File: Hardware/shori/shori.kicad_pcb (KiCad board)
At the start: 4 copper layers, 93 x 39.4 mm, 54 parts, among them J1 Conn_02x03_Top_Bottom, J2 SWD_Header, J3 UART_Header, J5 AudioJack3, U1 STM32F405RGT6, U2 AP2112K-3.3, U3 PCM3060PWR, U4 NE5532, Y1 16MHz

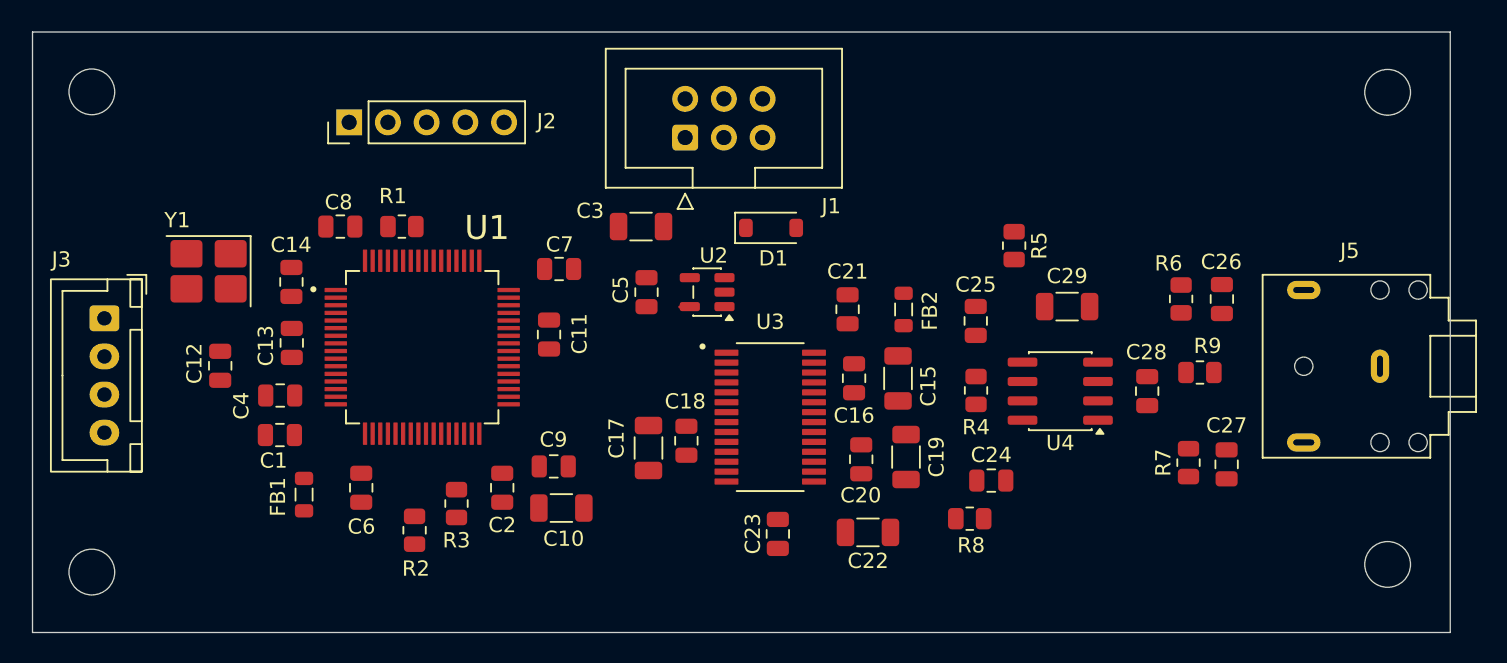
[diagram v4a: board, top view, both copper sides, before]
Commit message: Routes Oscillator, Gamen and Programming header.
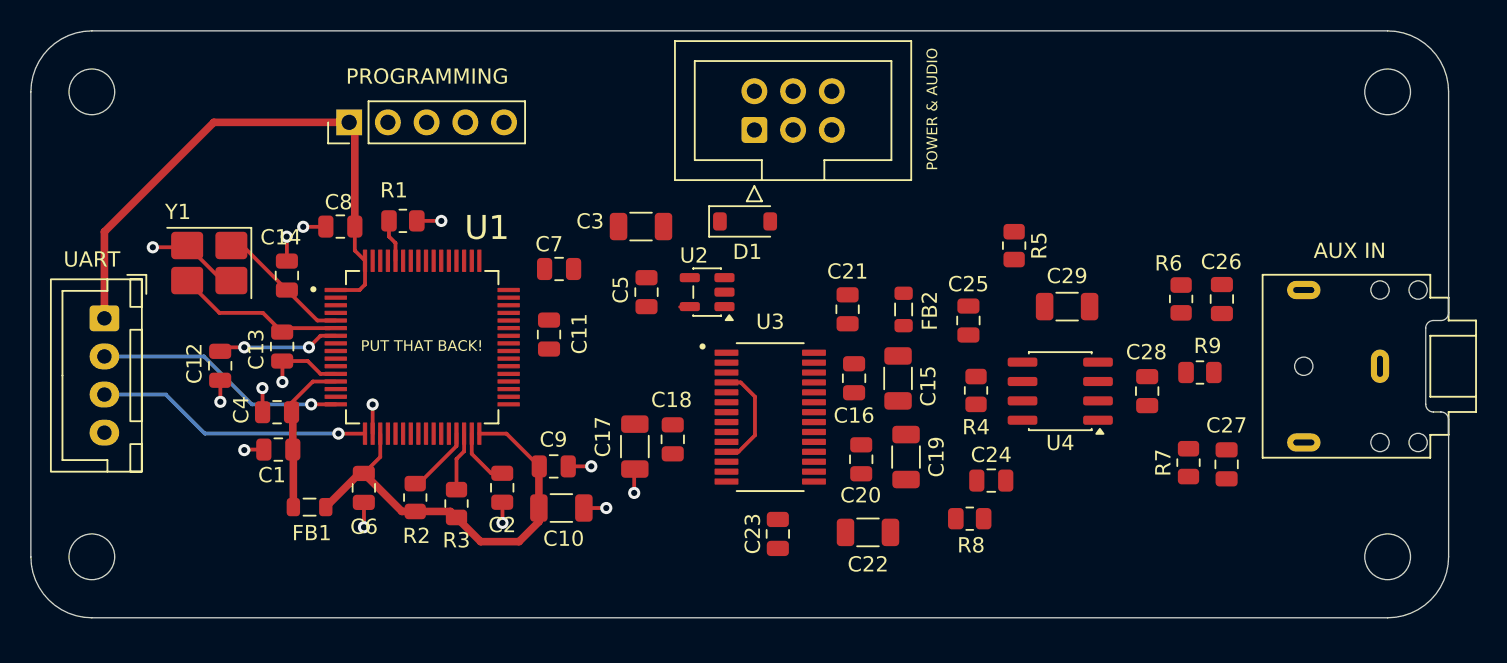
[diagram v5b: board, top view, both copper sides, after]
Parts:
- AUX IN: renamed from J5
- POWER & AUDIO: renamed from J1
- moved POWER & AUDIO 4.57 mm to (153.0, 74.5)
- moved R2 2.15 mm to (130.7, 98.6)
- moved D1 1.76 mm to (152.3, 80.5)
- moved C4 1.11 mm to (121.7, 93.0)
- moved H4 1.00 mm to (109.5, 102.5)
- moved C1 0.96 mm to (121.7, 95.5)
- moved C18 0.90 mm to (147.6, 94.8)
- moved C17 0.90 mm to (145.1, 95.3)
- moved FB1 0.90 mm to (123.8, 99.2), turned to 180 degrees
- moved C13 0.67 mm to (122.0, 88.7)
- moved Y1 0.54 mm to (117.2, 83.2)
- moved C14 0.51 mm to (122.3, 84.0)
- moved H2 0.50 mm to (194.5, 102.5)
- moved C25 0.48 mm to (167.0, 87.0)
- moved R1 0.38 mm to (129.9, 80.5)
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- renumbered J2 to PROGRAMMING, J3 to UART
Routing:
- net +3.3V: track 0.71 -> 67.4 mm
- net GND: track 0.00 -> 29.9 mm, vias 0 -> 14
- net /UART_RX: track 0.00 -> 18.2 mm, vias 0 -> 1
- net /UART_TX: track 0.00 -> 16.5 mm, vias 0 -> 1
- net /LOAD_CAP13: track 0.00 -> 10.9 mm
- net +3.3VA: track 0.00 -> 10.2 mm
- net /LOAD_CAP14: track 0.00 -> 8.89 mm
- net /NRST: track 0.00 -> 8.00 mm, vias 0 -> 2
- net /I2S_LRCLK: track 0.00 -> 7.11 mm
- net /I2C_SCL: track 0.00 -> 4.54 mm
- net /I2C_SDA: track 0.00 -> 3.88 mm
- net /VCAP_1: track 0.00 -> 3.85 mm
- net /BOOT0_R: track 0.00 -> 2.79 mm
- added copper zone on In1.Cu, net GND
- added copper zone on In2.Cu, net GND
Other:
- board size 93 x 39.4 mm -> 93 x 38.5 mm
- board text added: "PUT THAT BACK!"

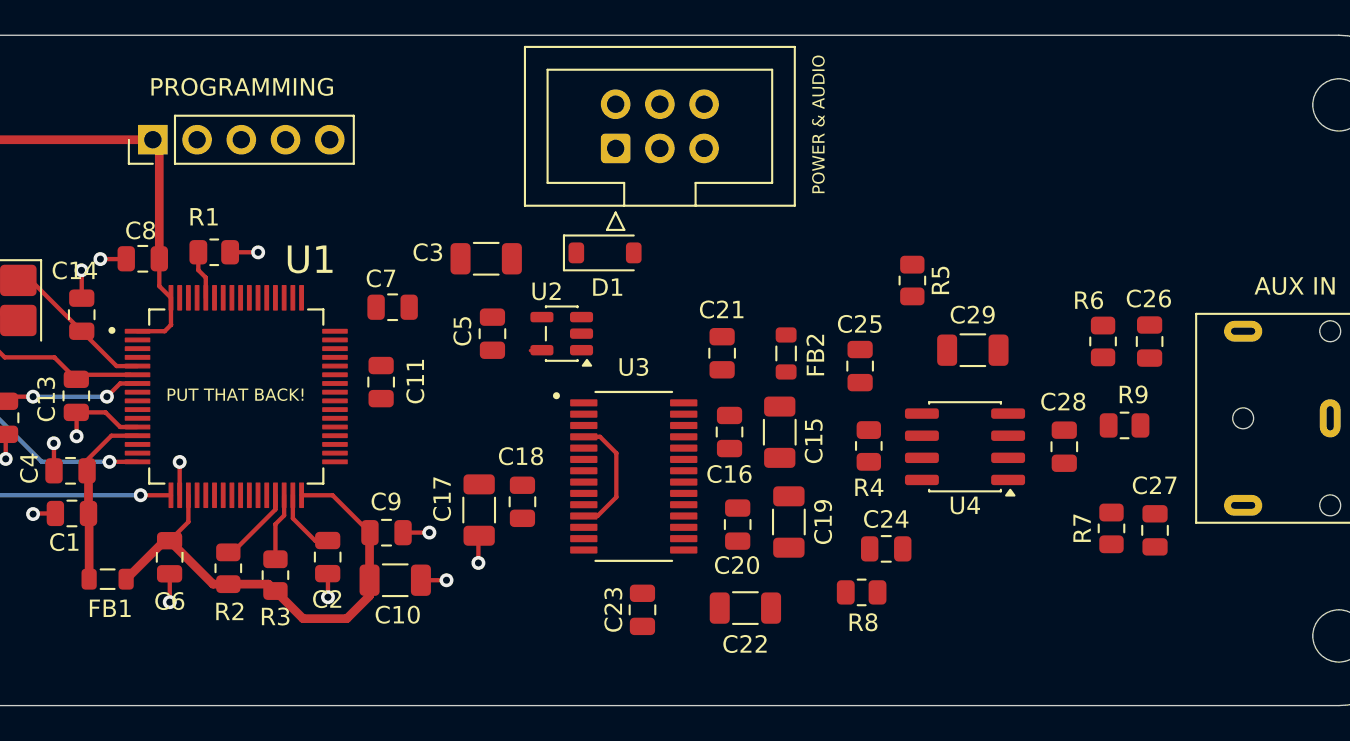
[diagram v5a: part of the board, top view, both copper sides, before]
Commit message: Rough Analog Routing complete for shori
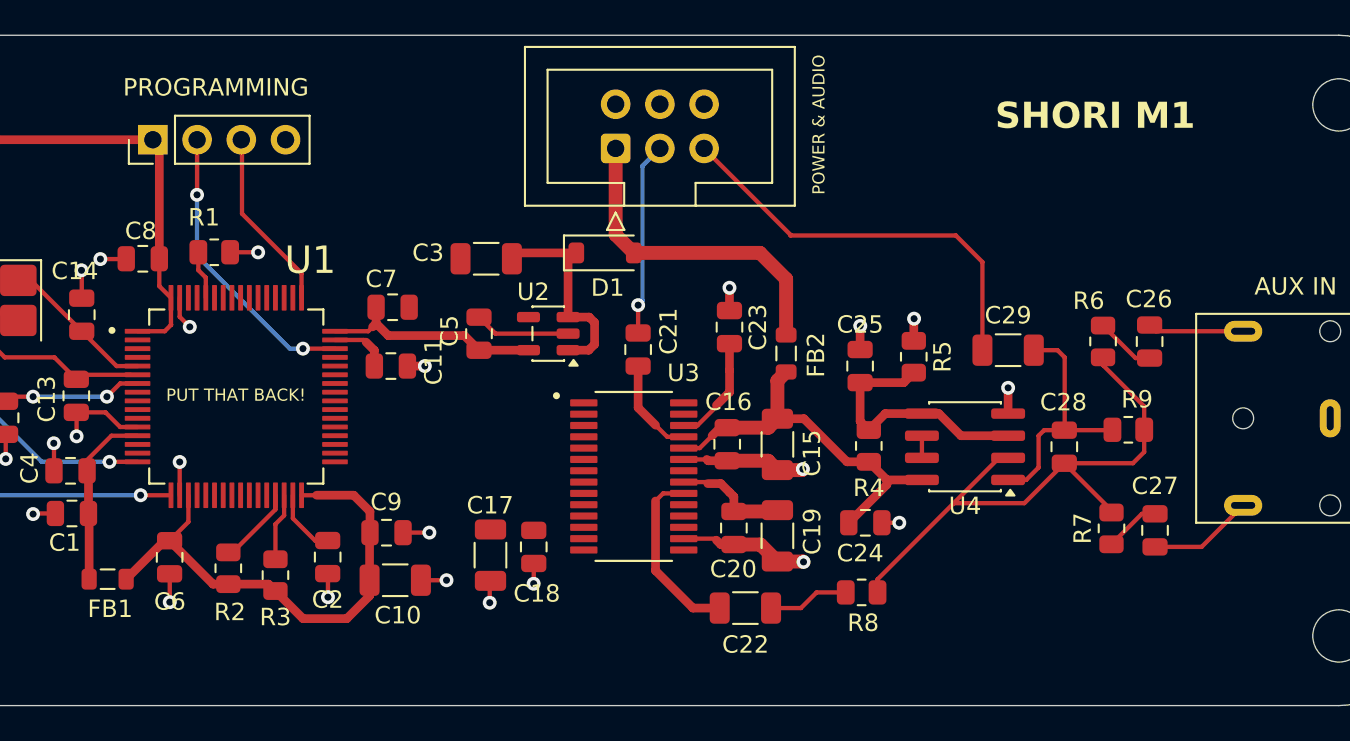
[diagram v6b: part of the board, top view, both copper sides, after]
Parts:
- PROGRAMMING: footprint Connector_PinHeader_2.54mm:PinHeader_1x05_P2.54mm_Vertical -> Connector_PinHeader_2.54mm:PinHeader_1x04_P2.54mm_Vertical
- moved C23 17.0 mm to (159.5, 84.8), turned to 90 degrees
- moved C21 4.83 mm to (154.2, 86.0)
- moved R5 4.38 mm to (170.1, 86.5)
- moved C18 2.67 mm to (148.3, 97.4)
- moved C17 2.67 mm to (145.8, 97.9)
- moved C29 2.03 mm to (175.5, 86.1)
- moved C24 1.92 mm to (167.3, 96.0)
- moved C11 1.08 mm to (140.1, 87.0), turned to 180 degrees
- moved C19 1.03 mm to (162.2, 96.8)
- moved U2 0.77 mm to (149.1, 85.1)
- moved C5 0.77 mm to (145.1, 85.1)
- moved C16 0.71 mm to (159.4, 91.5)
- moved C15 0.71 mm to (162.2, 91.5)
- moved R9 0.33 mm to (182.4, 90.7)
- moved C20 0.29 mm to (159.8, 96.3)
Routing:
- net /AUX_MIX: track 0.00 -> 33.7 mm
- net GND: track 29.9 -> 60.1 mm, vias 14 -> 24
- net /AUDIO_OUT: track 0.00 -> 23.8 mm
- net +5VA: track 0.00 -> 22.1 mm
- net +5V: track 0.08 -> 19.1 mm
- net /SWDIO: track 0.00 -> 16.8 mm, vias 0 -> 2
- net /VBIAS: track 0.00 -> 15.2 mm
- net /SUMMED_OUT: track 0.00 -> 14.4 mm
- net +3.3V: track 67.4 -> 81.0 mm
- net Net-(D1-K): track 0.00 -> 12.3 mm
- net /AUDIO_IN: track 0.00 -> 11.1 mm, vias 0 -> 1
- net /SWCLK: track 0.00 -> 10.5 mm
- net /VOUTL+: track 0.00 -> 10.4 mm
- net /I2S_LRCLK: track 7.11 -> 0.00 mm
- net /VCOM: track 0.00 -> 6.61 mm
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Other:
- board text added: "SHORI M1"

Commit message: saved previous commit
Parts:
- removed AUX IN: AudioJack3, Connector_Audio:Jack_3.5mm_CUI_SJ1-3523N_Horizontal
- removed POWER & AUDIO: Conn_02x03_Top_Bottom, Connector_IDC:IDC-Header_2x03_P2.54mm_Vertical
- removed PROGRAMMING: SWD_Header, Connector_PinHeader_2.54mm:PinHeader_1x04_P2.54mm_Vertical
- removed U1: STM32F405RGT6, My footprints:QFP50P1200X1200X160-64N
- removed UART: UART_Header, Connector_JST:JST_XH_B4B-XH-A_1x04_P2.50mm_Vertical
- added C30: 10uF, Capacitor_SMD:C_0805_2012Metric, F.Cu at (164.3, 104.5)
- added J1: Conn_01x03, Connector_JST:JST_EH_S3B-EH_1x03_P2.50mm_Horizontal, F.Cu at (132.7, 80.2)
- added J2: SWD_Header, Connector_PinHeader_2.54mm:PinHeader_1x05_P2.54mm_Vertical, F.Cu at (169.5, 74.7)
- added J3: UART_Header, Connector_JST:JST_XH_S4B-XH-A-1_1x04_P2.50mm_Horizontal, F.Cu at (166.8, 111.7)
- added J4: Conn_01x03, Connector_JST:JST_EH_S3B-EH_1x03_P2.50mm_Horizontal, F.Cu at (132.7, 90.6)
- added J5: AudioJack3, Connector_Audio:Jack_3.5mm_CUI_SJ1-3523N_Horizontal, F.Cu at (155.8, 117.5)
- added J6: Conn_01x03, Connector_JST:JST_EH_S3B-EH_1x03_P2.50mm_Horizontal, F.Cu at (132.7, 100.9)
- added U5: TPS73733DCQR, MyFootprints:IC_TPS73733DCQR, F.Cu at (134.1, 107.7)
- C10: value 10uF -> 100uF
- C3: value 10μF -> 4.7uF
- U2: value AP2112K-3.3 -> STM32H750VBTx; footprint Package_TO_SOT_SMD:SOT-23-5 -> Package_QFP:LQFP-100_14x14mm_P0.5mm
- U3: footprint My footprints:SOP65P640X120-28N -> MyFootprints:SOP65P640X120-28N
- moved R1 54.4 mm to (165.1, 122.0)
- moved H2 53.0 mm to (144.9, 83.8), turned to 0 degrees
- moved H1 49.7 mm to (144.9, 76.2)
- moved C29 49.6 mm to (144.0, 124.4), turned to 0 degrees
- moved U4 46.1 mm to (133.3, 115.1), turned to 0 degrees
- moved R6 43.9 mm to (169.5, 128.0), turned to 0 degrees
- moved FB2 43.8 mm to (138.0, 122.4), turned to 0 degrees
- moved R2 43.3 mm to (165.1, 125.0), turned to 0 degrees
- moved R3 42.9 mm to (165.1, 128.0), turned to 0 degrees
- moved Y1 40.9 mm to (132.4, 121.2), turned to 0 degrees
- moved C14 40.6 mm to (155.4, 107.5), turned to 0 degrees
- moved H3 40.4 mm to (144.9, 91.3)
- moved C12 39.2 mm to (155.4, 101.5), turned to 0 degrees
- moved R5 38.5 mm to (169.5, 125.0), turned to 0 degrees
- moved R9 38.3 mm to (173.9, 128.0), turned to 0 degrees
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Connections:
- C12 pad 1: /NRST -> /BOOT0_R
- U2 pad 1: Net-(D1-K) -> unconnected-(U2-PE2-Pad1)
- U2 pad 2: GND -> unconnected-(U2-PE3-Pad2)
- U2 pad 3: Net-(D1-K) -> unconnected-(U2-PE4-Pad3)
- U2 pad 5: +3.3V -> unconnected-(U2-PE6-Pad5)
- U3 pad 15: /NRST -> /BOOT0_R
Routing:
- net +3.3V: track 81.0 -> 0.00 mm
- net GND: track 60.1 -> 0.00 mm, vias 24 -> 0
- net /AUX_MIX: track 33.7 -> 0.00 mm
- net /AUDIO_OUT: track 23.8 -> 0.00 mm
- net +5VA: track 22.1 -> 0.00 mm
- net +5V: track 19.1 -> 0.00 mm
- net /UART_RX: track 18.2 -> 0.00 mm, vias 1 -> 0
- net /SWDIO: track 16.8 -> 0.00 mm, vias 2 -> 0
- net /UART_TX: track 16.5 -> 0.00 mm, vias 1 -> 0
- net /VBIAS: track 15.2 -> 0.00 mm
- net /SUMMED_OUT: track 14.4 -> 0.00 mm
- net Net-(D1-K): track 12.3 -> 0.00 mm
- net /AUDIO_IN: track 11.1 -> 0.00 mm, vias 1 -> 0
- net /LOAD_CAP13: track 10.9 -> 0.00 mm
- net /SWCLK: track 10.5 -> 0.00 mm
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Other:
- board size 93 x 38.5 mm -> 13 x 1.4 mm
- board text removed: "PUT THAT BACK!"
- board text removed: "SHORI M1"

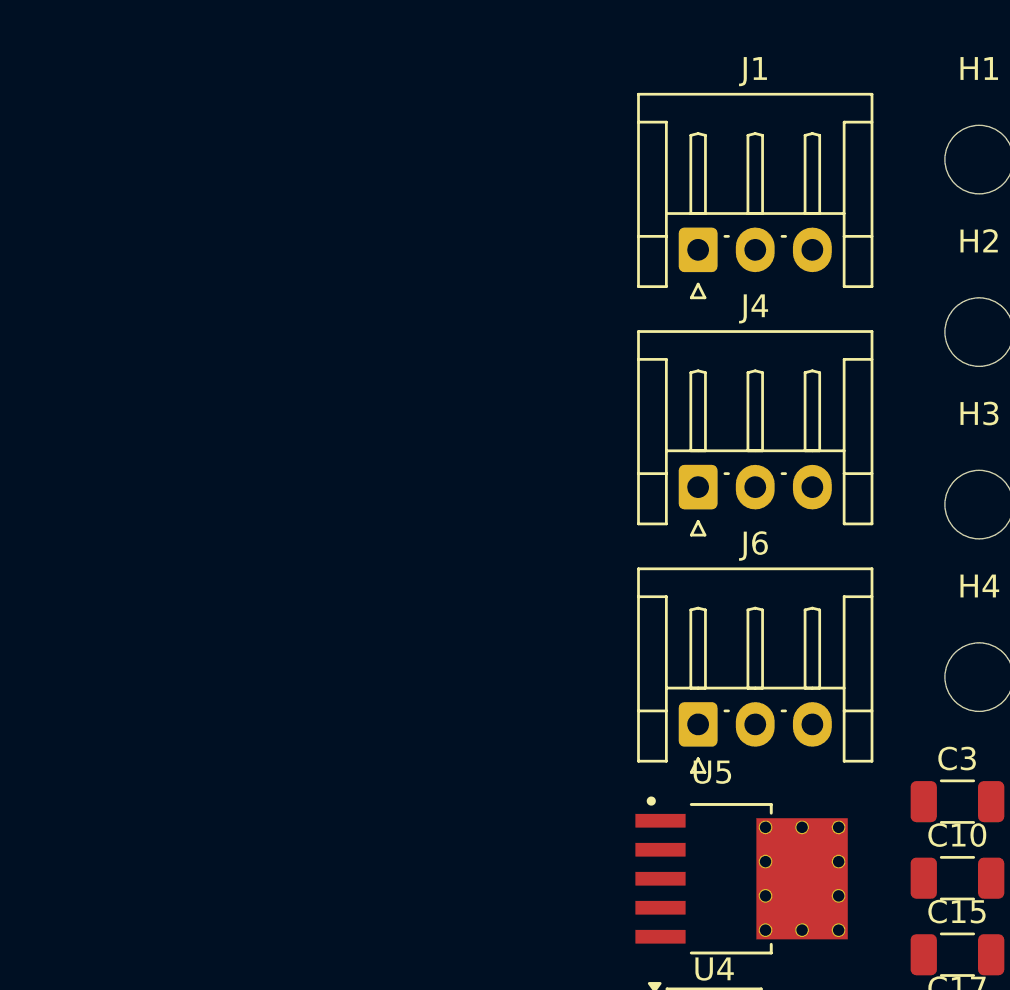
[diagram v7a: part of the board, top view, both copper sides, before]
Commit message: Rev 2 mcu data lines and new shoyu molex connectors
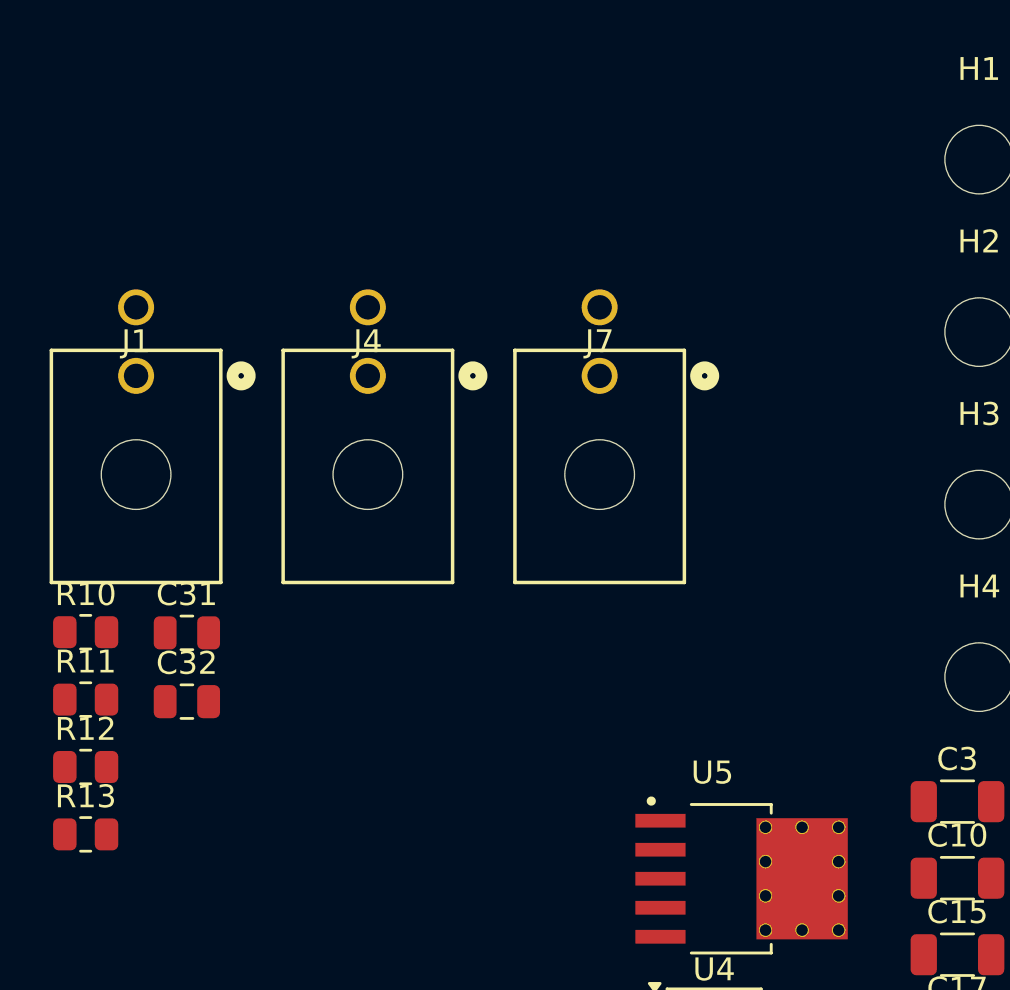
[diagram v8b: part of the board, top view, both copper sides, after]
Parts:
- removed J6: Conn_01x03, Connector_JST:JST_EH_S3B-EH_1x03_P2.50mm_Horizontal
- added C31: 100nF, Capacitor_SMD:C_0805_2012Metric, F.Cu at (110.3, 96.9)
- added C32: 1uF, Capacitor_SMD:C_0805_2012Metric, F.Cu at (110.3, 99.9)
- added J7: 430450200, MyFootprints:CONN_SD-43045-001_02_MOL, F.Cu at (128.3, 85.7)
- added R10: 22Ω, Resistor_SMD:R_0805_2012Metric, F.Cu at (105.8, 96.9)
- added R11: 22o, Resistor_SMD:R_0805_2012Metric, F.Cu at (105.8, 99.9)
- added R12: 22o, Resistor_SMD:R_0805_2012Metric, F.Cu at (105.8, 102.8)
- added R13: 22o, Resistor_SMD:R_0805_2012Metric, F.Cu at (105.8, 105.8)
- C1: value 10μF -> 4.7uf
- C3: value 4.7uF -> 10uF
- J1, J4: value Conn_01x03 -> 430450200; footprint Connector_JST:JST_EH_S3B-EH_1x03_P2.50mm_Horizontal -> MyFootprints:CONN_SD-43045-001_02_MOL
- R3: value 2.2k -> 2.2K
- moved J1 25.2 mm to (108.1, 85.7)
- moved J4 15.3 mm to (118.2, 85.7)
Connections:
- C12 pad 1: /BOOT0_R -> /NRST
- U2 pad 12: unconnected-(U2-PH0-Pad12) -> /LOAD_CAP14
- U2 pad 13: unconnected-(U2-PH1-Pad13) -> /LOAD_CAP13
- U2 pad 14: /BOOT0_R -> /NRST
- U2 pad 20: unconnected-(U2-VREF+-Pad20) -> +3.3V
- U2 pad 22: /UART_TX -> Net-(U2-PA0)
- U2 pad 23: /UART_RX -> Net-(U2-PA1)
- U2 pad 51: /I2S_BCLK -> /I2S_SR_LRCLK
- U2 pad 52: /I2S_LRCLK -> /I2S_SR_BCLK
- U2 pad 53: /I2S_ADC_DATA -> /I2S_SR_ADC_DATA
- U2 pad 54: /I2S_DAC_DATA -> /I2S_SR_DAC_DATA
- U3 pad 15: /BOOT0_R -> /NRST
